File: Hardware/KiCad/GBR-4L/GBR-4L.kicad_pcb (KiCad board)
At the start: 4 copper layers, 160 x 100 mm, 188 parts, among them J1 USB4105-GF-A, J101 EM7565 M.2 Key B socket, J102 MODEM_CONTROL, J201 EM7565 M.2 Key B socket, J202 MODEM_CONTROL, J301 EM7565 M.2 Key B socket, J302 MODEM_CONTROL, J401 EM7565 M.2 Key B socket, J402 MODEM_CONTROL, J511 2452808-1 nano-SIM, J521 2452808-1 nano-SIM, J531 2452808-1 nano-SIM, J541 2452808-1 nano-SIM, J701 12V INPUT 5A, Q701 30V P-MOSFET low-RDS(on), Q911 MMBT3906, Q921 MMBT3906, Q931 MMBT3906, Q941 MMBT3906, SW911 MODEM 1 RESET, SW912 MODEM 1 RF DISABLE, SW921 MODEM 2 RESET, SW922 MODEM 2 RF DISABLE, SW931 MODEM 3 RESET, SW932 MODEM 3 RF DISABLE, SW941 MODEM 4 RESET, SW942 MODEM 4 RF DISABLE, U1 USBLC6-2SC6, U11 LOW-CAP SIM ESD ARRAY, U12 LOW-CAP SIM ESD ARRAY, U13 LOW-CAP SIM ESD ARRAY, U14 LOW-CAP SIM ESD ARRAY, U2 USB2514Bi-I/M2, U21 TPS56339DDCR, U22 TPS56339DDCR, U23 TPS56339DDCR, U24 TPS56339DDCR, U25 TPS56339DDCR, Y1 24MHz

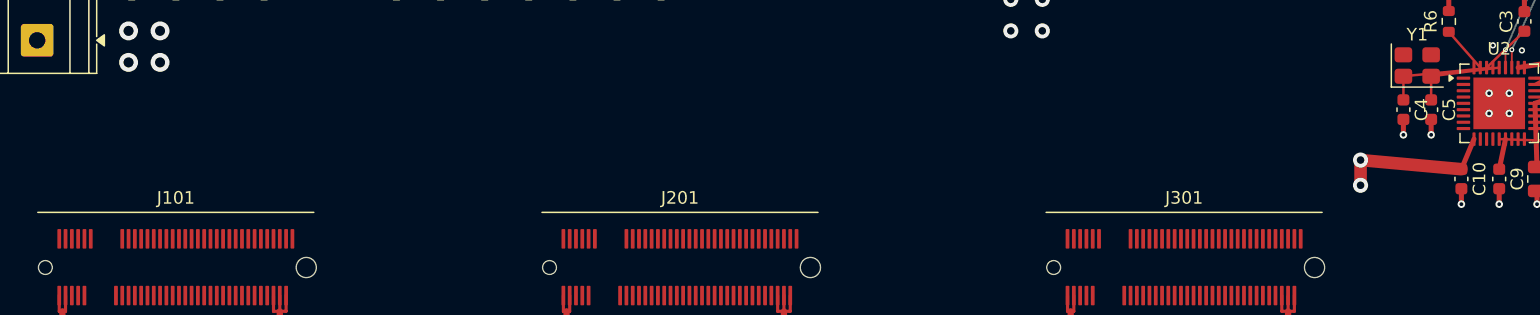
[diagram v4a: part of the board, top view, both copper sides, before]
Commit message: Route USB hub port 1 to modem slot
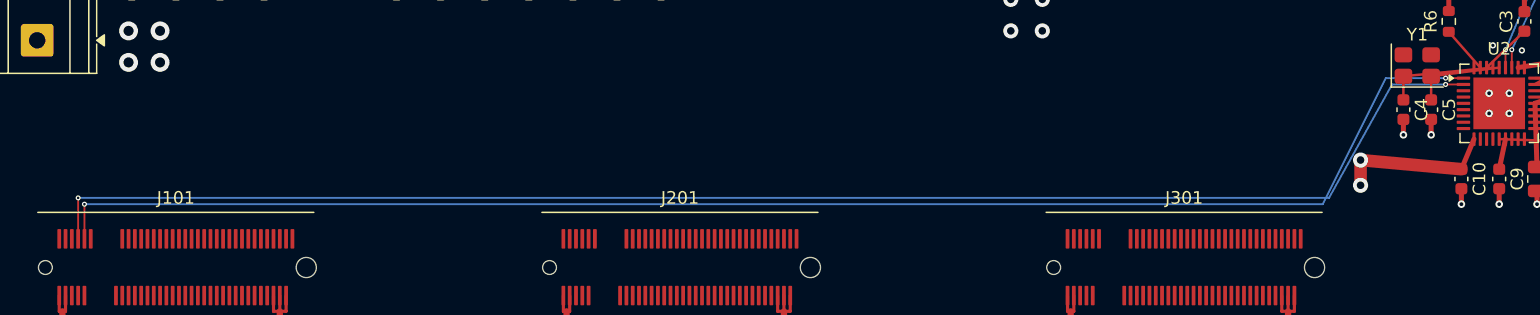
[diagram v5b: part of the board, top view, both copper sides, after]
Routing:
- net USB_M1_D+: track 0.00 -> 118.5 mm, vias 0 -> 2
- net USB_M1_D-: track 0.00 -> 118.3 mm, vias 0 -> 2
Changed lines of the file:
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@@
+	)
+	(segment
+		(start 32.25 62.5)
+		(end 32.25 65.75)
+		(width 0.15)
+		(layer "F.Cu")
+		(net "USB_M1_D+")
+	)
+	(segment
+		(start 142.162 53.5)
+		(end 140.75 53.5)
+		(width 0.15)
+		(layer "F.Cu")
+		(net "USB_M1_D+")
+	)
+	(via
+		(at 32.25 62.5)
+		(size 0.4)
+		(drill 0.2)
+		(layers "F.Cu" "B.Cu")
+		(net "USB_M1_D+")
+	)
+	(via
+		(at 140.75 53.5)
+		(size 0.4)
+		(drill 0.2)
+		(layers "F.Cu" "B.Cu")
+		(net "USB_M1_D+")
+	)
+	(segment
+		(start 140.75 53.5)
+		(end 136.5 53.5)
+		(width 0.15)
+		(layer "B.Cu")
+		(net "USB_M1_D+")
+	)
+	(segment
+		(start 136.5 53.5)
+		(end 131.5 62.5)
+		(width 0.15)
+		(layer "B.Cu")
+		(net "USB_M1_D+")
+	)
+	(segment
+		(start 131.5 62.5)
+		(end 32.25 62.5)
+		(width 0.15)
+		(layer "B.Cu")
+		(net "USB_M1_D+")
+	)
+	(segment
+		(start 32.75 63)
+		(end 32.75 65.75)
+		(width 0.15)
+		(layer "F.Cu")
+		(net "USB_M1_D-")
+	)
+	(segment
+		(start 142.162 53)
+		(end 140.75 53)
+		(width 0.15)
+		(layer "F.Cu")
+		(net "USB_M1_D-")
+	)
+	(via
+		(at 140.75 53)
+		(size 0.4)
+		(drill 0.2)
+		(layers "F.Cu" "B.Cu")
+		(net "USB_M1_D-")
+	)
+	(via
+		(at 32.75 63)
+		(size 0.4)
+		(drill 0.2)
+		(layers "F.Cu" "B.Cu")
+		(net "USB_M1_D-")
+	)
+	(segment
+		(start 136 53)
+		(end 131 63)
+		(width 0.15)
+		(layer "B.Cu")
+		(net "USB_M1_D-")
+	)
+	(segment
+		(start 140.75 53)
+		(end 136 53)
+		(width 0.15)
+		(layer "B.Cu")
+		(net "USB_M1_D-")
+	)
+	(segment
+		(start 131 63)
+		(end 32.75 63)
+		(width 0.15)
+		(layer "B.Cu")
+		(net "USB_M1_D-")
 	)
 	(segment

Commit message: Route USB hub port 2 to modem slot
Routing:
- net USB_M2_D+: track 0.00 -> 77.8 mm, vias 0 -> 2
- net USB_M2_D-: track 0.00 -> 77.6 mm, vias 0 -> 2
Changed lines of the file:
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@@
+	)
+	(segment
+		(start 72.75 62)
+		(end 72.75 65.75)
+		(width 0.15)
+		(layer "F.Cu")
+		(net "USB_M2_D-")
+	)
+	(segment
+		(start 142.162 54)
+		(end 140.75 54)
+		(width 0.15)
+		(layer "F.Cu")
+		(net "USB_M2_D-")
+	)
+	(via
+		(at 140.75 54)
+		(size 0.4)
+		(drill 0.2)
+		(layers "F.Cu" "B.Cu")
+		(net "USB_M2_D-")
+	)
+	(via
+		(at 72.75 62)
+		(size 0.4)
+		(drill 0.2)
+		(layers "F.Cu" "B.Cu")
+		(net "USB_M2_D-")
+	)
+	(segment
+		(start 140.75 54)
+		(end 137 54)
+		(width 0.15)
+		(layer "B.Cu")
+		(net "USB_M2_D-")
+	)
+	(segment
+		(start 137 54)
+		(end 132 62)
+		(width 0.15)
+		(layer "B.Cu")
+		(net "USB_M2_D-")
+	)
+	(segment
+		(start 132 62)
+		(end 72.75 62)
+		(width 0.15)
+		(layer "B.Cu")
+		(net "USB_M2_D-")
+	)
+	(segment
+		(start 142.162 54.5)
+		(end 140.75 54.5)
+		(width 0.15)
+		(layer "F.Cu")
+		(net "USB_M2_D+")
+	)
+	(segment
+		(start 72.25 61.5)
+		(end 72.25 65.75)
+		(width 0.15)
+		(layer "F.Cu")
+		(net "USB_M2_D+")
+	)
+	(via
+		(at 140.75 54.5)
+		(size 0.4)
+		(drill 0.2)
+		(layers "F.Cu" "B.Cu")
+		(net "USB_M2_D+")
+	)
+	(via
+		(at 72.25 61.5)
+		(size 0.4)
+		(drill 0.2)
+		(layers "F.Cu" "B.Cu")
+		(net "USB_M2_D+")
+	)
+	(segment
+		(start 132.5 61.5)
+		(end 72.25 61.5)
+		(width 0.15)
+		(layer "B.Cu")
+		(net "USB_M2_D+")
+	)
+	(segment
+		(start 140.75 54.5)
+		(end 137.5 54.5)
+		(width 0.15)
+		(layer "B.Cu")
+		(net "USB_M2_D+")
+	)
+	(segment
+		(start 137.5 54.5)
+		(end 132.5 61.5)
+		(width 0.15)
+		(layer "B.Cu")
+		(net "USB_M2_D+")
 	)
 	(segment
